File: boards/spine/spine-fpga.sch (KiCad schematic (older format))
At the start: 1 part, among them U2 iCE40-HX1K-TQ144

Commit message: Get the BOM started
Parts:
- U2: MfgId (none) -> ICE40HX1K-TQ144; MfrId (none) -> Lattice; RefPrice1k (none) -> 4.5703; Vend1 (none) -> Digikey; Vend1Id (none) -> 220-1565-ND
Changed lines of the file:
@@
 F 1 "iCE40-HX1K-TQ144" H 1800 1800 60  0000 L CNN
 F 2 "" H 1600 1650 60  0000 C CNN
-F 3 "" H 1600 1650 60  0000 C CNN
+F 3 "http://www.latticesemi.com/~/media/LatticeSemi/Documents/DataSheets/iCE/iCE40LPHXFamilyDataSheet.pdf" H 1600 1650 60  0001 C CNN
+F 4 "4.5703" H 1600 1650 60  0001 C CNN "RefPrice1k"
+F 5 "Lattice" H 1600 1650 60  0001 C CNN "MfrId"
+F 6 "ICE40HX1K-TQ144" H 1600 1650 60  0001 C CNN "MfgId"
+F 7 "220-1565-ND" H 1600 1650 60  0001 C CNN "Vend1Id"
+F 8 "Digikey" H 1600 1650 60  0001 C CNN "Vend1"
 	1    1600 1650
 	1    0    0    -1

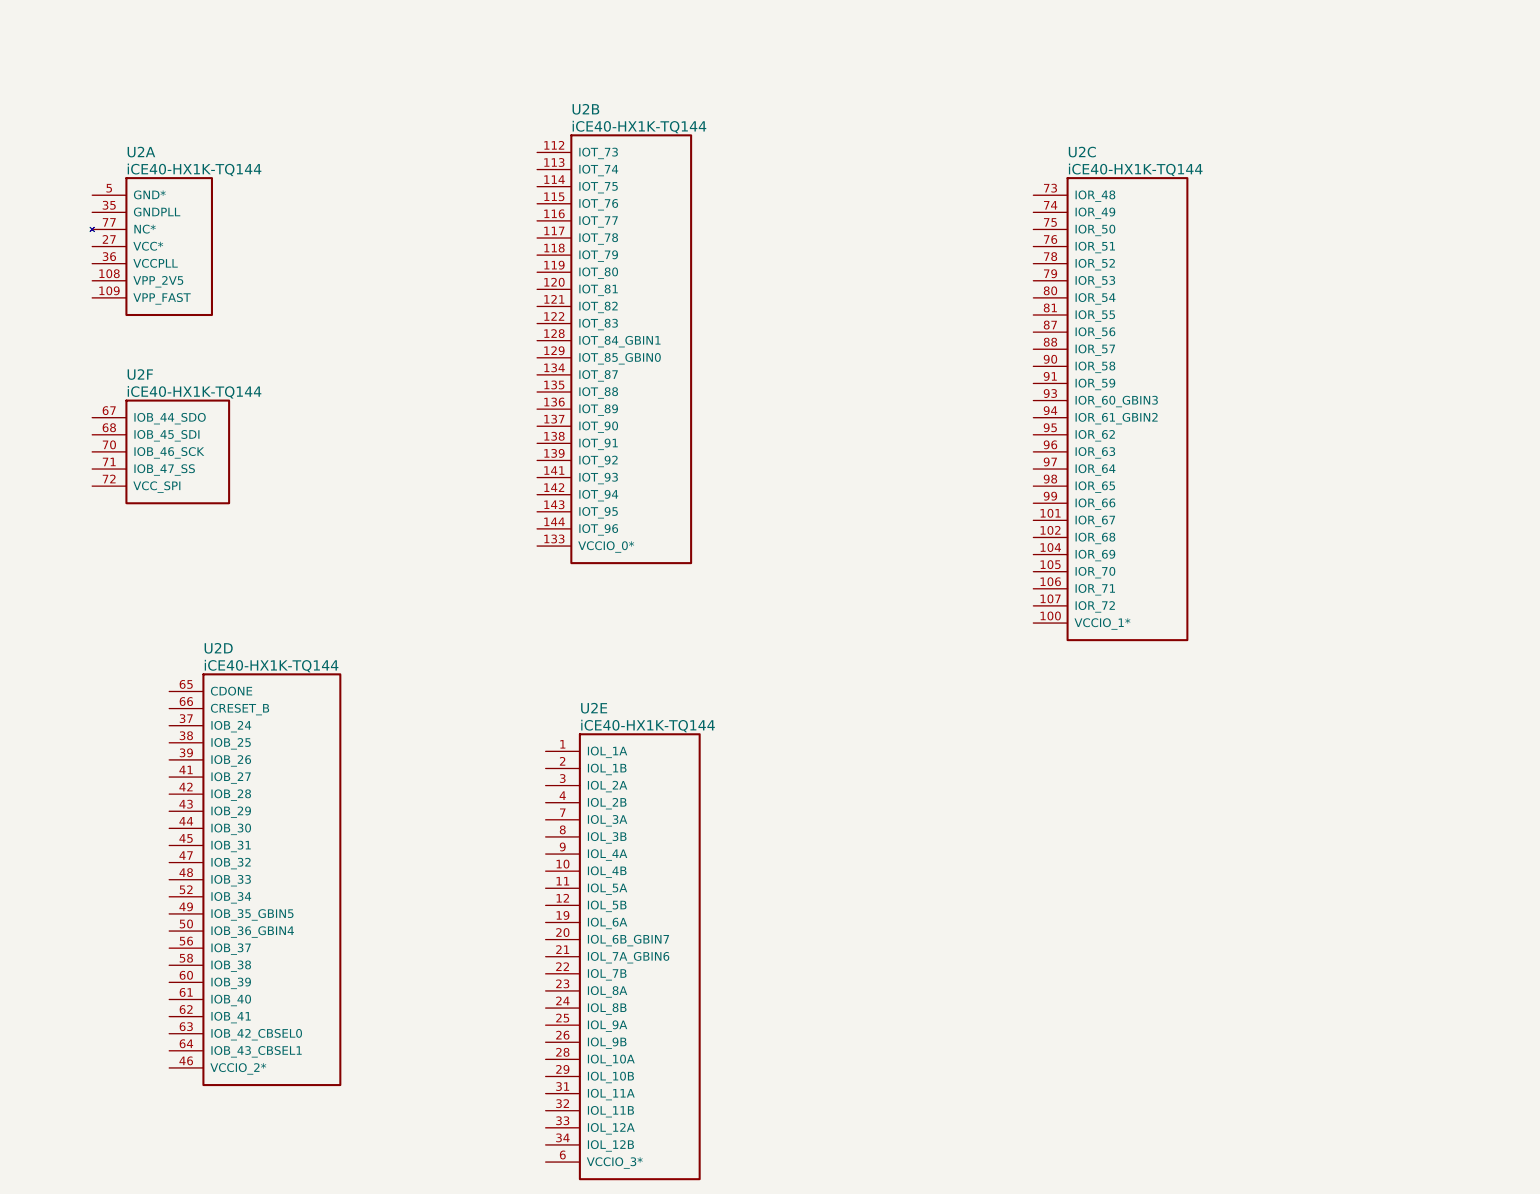
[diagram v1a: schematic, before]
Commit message: USB port: ESD, crystal, eeprom
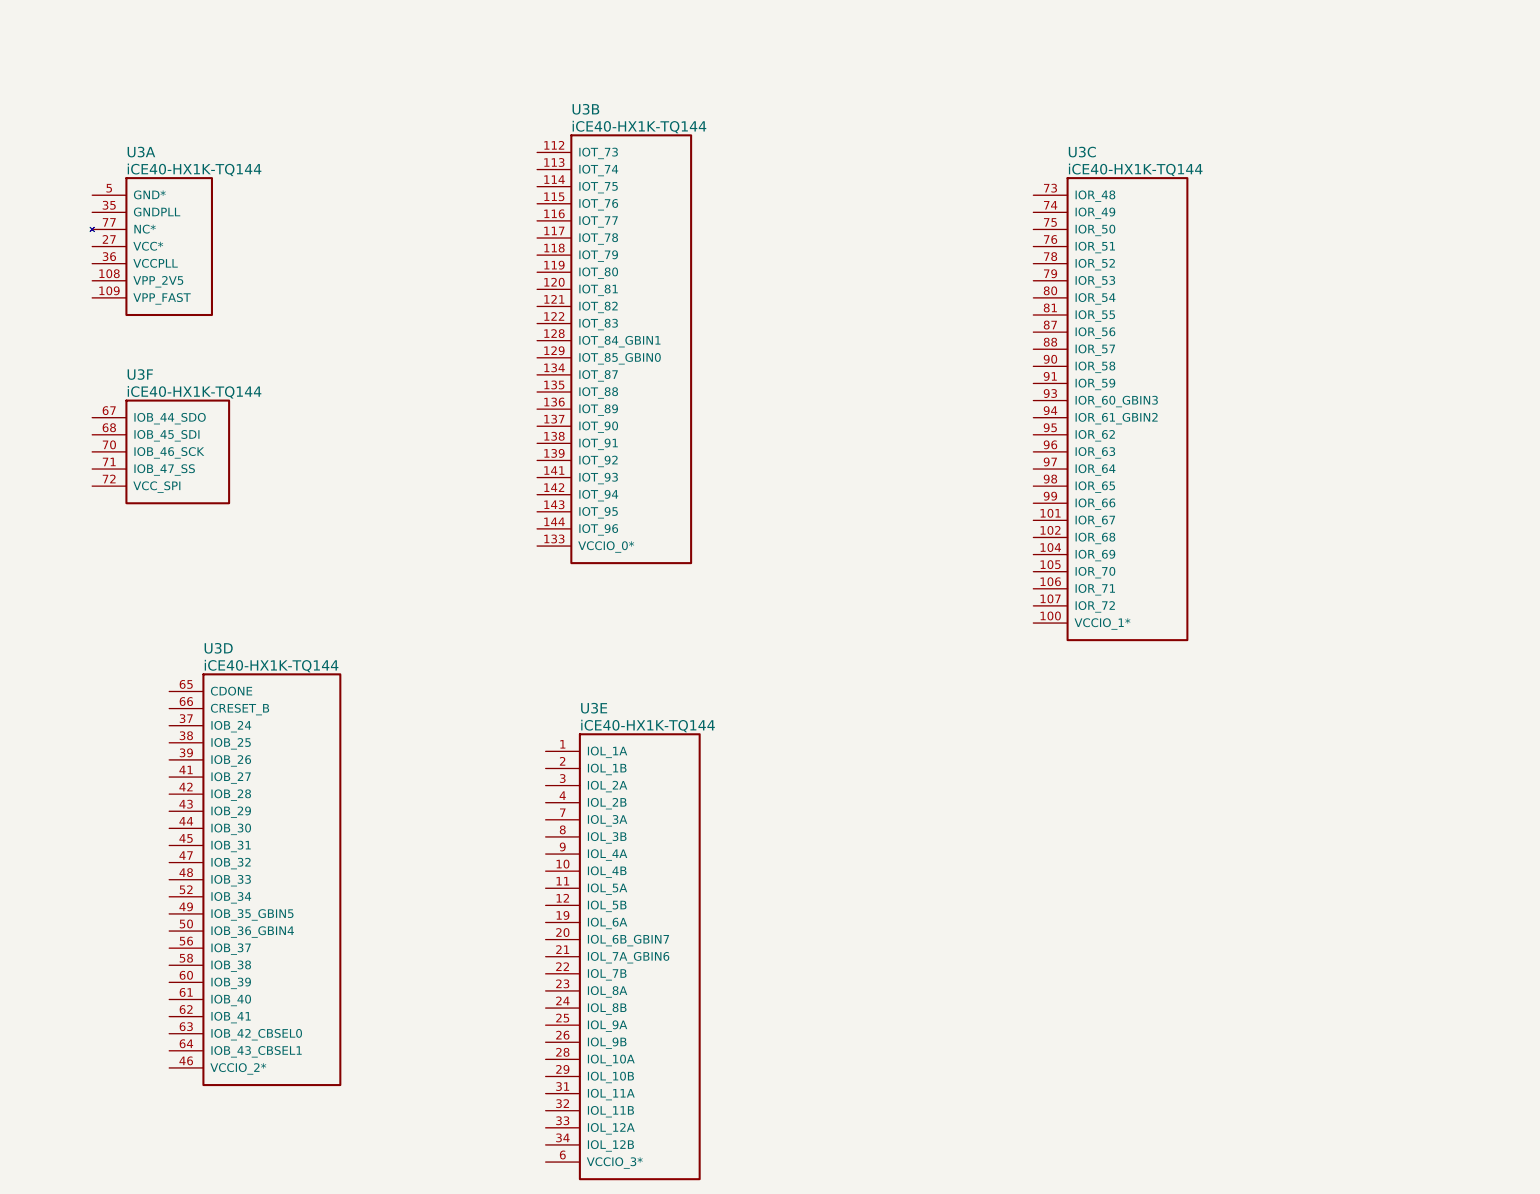
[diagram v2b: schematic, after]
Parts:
- renumbered U2 to U3
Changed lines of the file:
@@
 $EndDescr
 $Comp
-L iCE40-HX1K-TQ144 U2
+L iCE40-HX1K-TQ144 U3
 U 1 1 5637E334
 P 1600 1650
-F 0 "U2" H 1800 1900 60  0000 L CNN
+F 0 "U3" H 1800 1900 60  0000 L CNN
 F 1 "iCE40-HX1K-TQ144" H 1800 1800 60  0000 L CNN
 F 2 "" H 1600 1650 60  0000 C CNN
@@
 $EndComp
 $Comp
-L iCE40-HX1K-TQ144 U2
+L iCE40-HX1K-TQ144 U3
 U 2 1 5637E355
 P 4200 1400
-F 0 "U2" H 4400 1650 60  0000 L CNN
+F 0 "U3" H 4400 1650 60  0000 L CNN
 F 1 "iCE40-HX1K-TQ144" H 4400 1550 60  0000 L CNN
 F 2 "" H 4200 1400 60  0000 C CNN
@@
 $EndComp
 $Comp
-L iCE40-HX1K-TQ144 U2
+L iCE40-HX1K-TQ144 U3
 U 3 1 5637E37F
 P 7100 1650
-F 0 "U2" H 7300 1900 60  0000 L CNN
+F 0 "U3" H 7300 1900 60  0000 L CNN
 F 1 "iCE40-HX1K-TQ144" H 7300 1800 60  0000 L CNN
 F 2 "" H 7100 1650 60  0000 C CNN
@@
 $EndComp
 $Comp
-L iCE40-HX1K-TQ144 U2
+L iCE40-HX1K-TQ144 U3
 U 4 1 5637E3AD
 P 2050 4550
-F 0 "U2" H 2250 4800 60  0000 L CNN
+F 0 "U3" H 2250 4800 60  0000 L CNN
 F 1 "iCE40-HX1K-TQ144" H 2250 4700 60  0000 L CNN
 F 2 "" H 2050 4550 60  0000 C CNN
@@
 $EndComp
 $Comp
-L iCE40-HX1K-TQ144 U2
+L iCE40-HX1K-TQ144 U3
 U 5 1 5637E3E2
 P 4250 4900
-F 0 "U2" H 4450 5150 60  0000 L CNN
+F 0 "U3" H 4450 5150 60  0000 L CNN
 F 1 "iCE40-HX1K-TQ144" H 4450 5050 60  0000 L CNN
 F 2 "" H 4250 4900 60  0000 C CNN
@@
 $EndComp
 $Comp
-L iCE40-HX1K-TQ144 U2
+L iCE40-HX1K-TQ144 U3
 U 6 1 5637E41B
 P 1600 2950
-F 0 "U2" H 1800 3200 60  0000 L CNN
+F 0 "U3" H 1800 3200 60  0000 L CNN
 F 1 "iCE40-HX1K-TQ144" H 1800 3100 60  0000 L CNN
 F 2 "" H 1600 2950 60  0000 C CNN

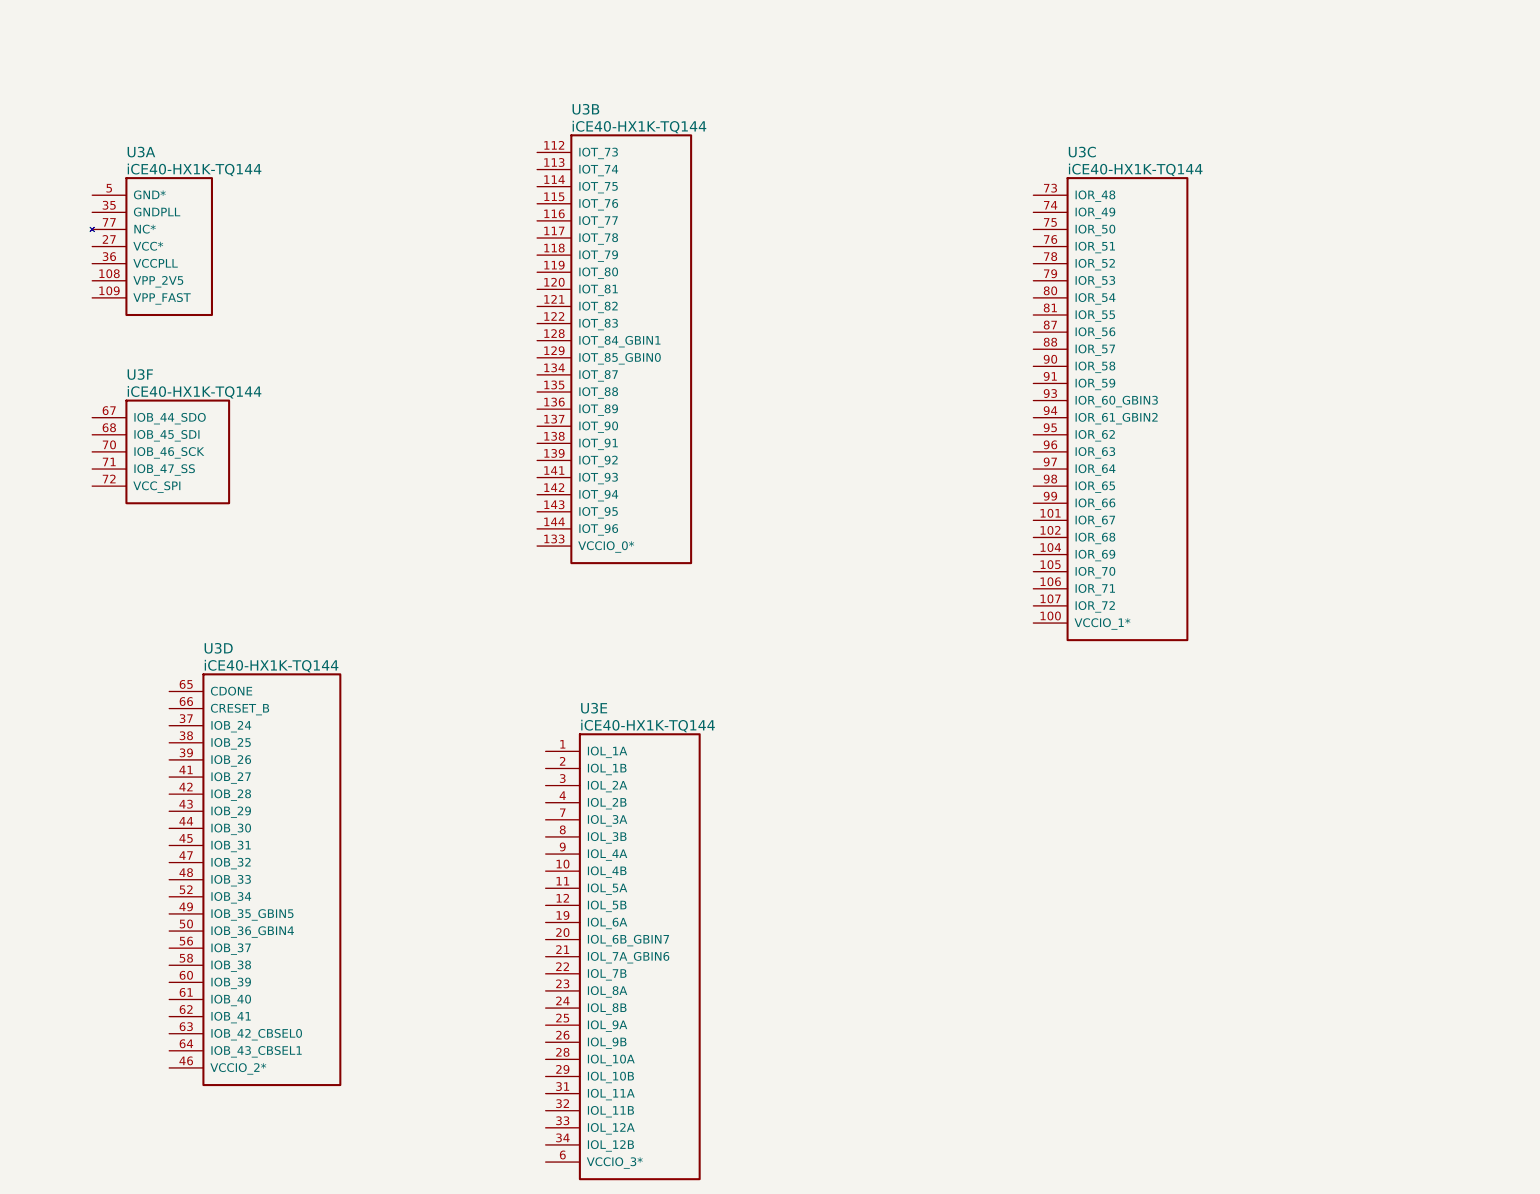
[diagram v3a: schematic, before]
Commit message: Getting the FPGA set up
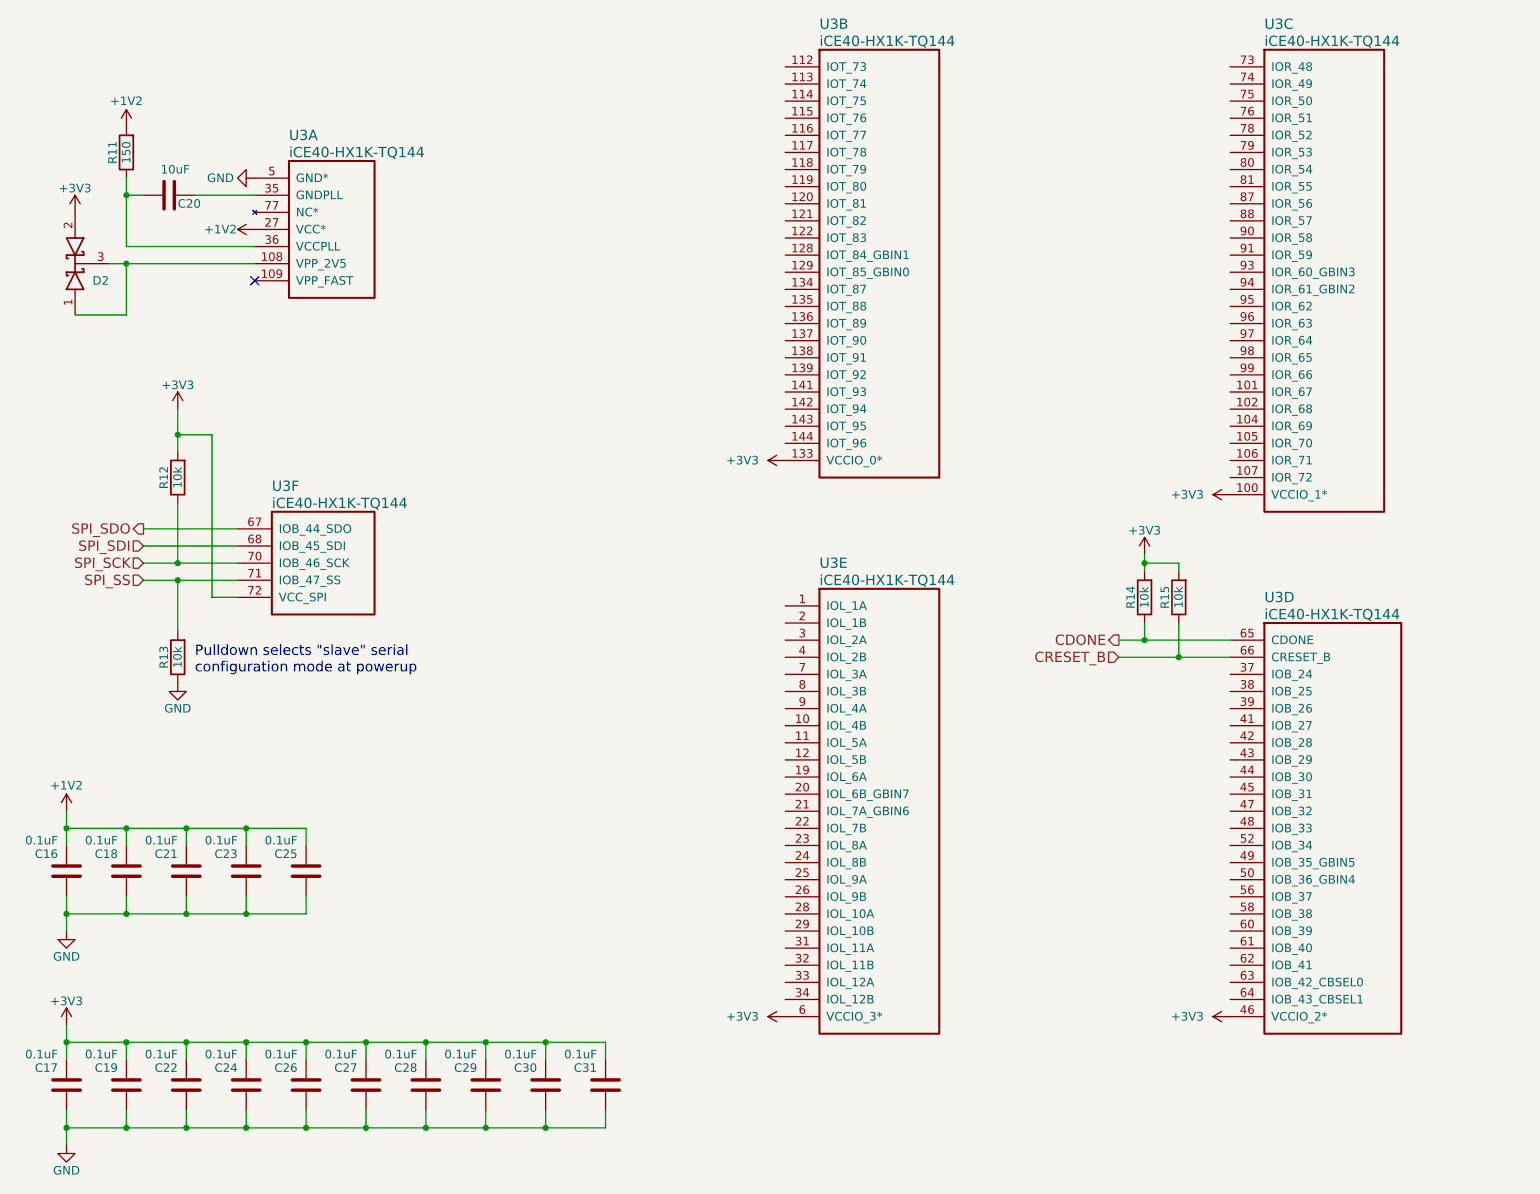
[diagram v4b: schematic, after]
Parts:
- added C16, C17, C18, C19, C21, C22, C23, C24, C25, C26, C27, C28, C29, C30, C31: 0.1uF, symbol C
- added C20: 10uF, symbol C
- added D2: BAT54 2x common cathode, symbol D_Schottky_x2_KCom_AAK
- added R11: 150, symbol R
- added R12, R13, R14, R15: 10k, symbol R
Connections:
- net GND: now reaches U3.103 (GND*), U3.13 (GND*), U3.132 (GND*), U3.14 (GND*), U3.140 (GND*), U3.5 (GND*), U3.59 (GND*), U3.69 (GND*), U3.86 (GND*)
- net GND: now also C16.1, C17.1, C18.1, C19.1, C21.1, C22.1, C23.1, C24.1, C25.1, C26.1, C27.1, C28.1, C29.1, C30.1, C31.1, R13.1
- net at U3.108 (VPP_2V5): now also D2.1 (A), D2.3 (K)
- net +1V2: now reaches U3.111 (VCC*), U3.27 (VCC*), U3.51 (VCC*), U3.92 (VCC*)
- net +1V2: now also C16.2, C18.2, C21.2, C23.2, C25.2, R11.2
- net at U3.35 (GNDPLL): now also C20.1
- net at U3.36 (VCCPLL): now also C20.2, R11.1
- net +3V3: now reaches U3.123 (VCCIO_0*), U3.133 (VCCIO_0*)
- net +3V3: now also U3.100 (VCCIO_1*), U3.30 (VCCIO_3*), U3.46 (VCCIO_2*), U3.57 (VCCIO_2*), U3.6 (VCCIO_3*), U3.72 (VCC_SPI), U3.89 (VCCIO_1*), C17.2, C19.2, C22.2, C24.2, C26.2, C27.2, C28.2, C29.2, C30.2, C31.2, D2.2 (A), R12.2, R14.2, R15.2
- net CDONE: now reaches U3.65 (CDONE)
- net CDONE: now also R14.1
- net CRESET_B: now reaches U3.66 (CRESET_B)
- net CRESET_B: now also R15.1
- net SPI_SDO: now reaches U3.67 (IOB_44_SDO)
- net SPI_SDI: now reaches U3.68 (IOB_45_SDI)
- net SPI_SCK: now reaches U3.70 (IOB_46_SCK)
- net SPI_SCK: now also R12.1
- net SPI_SS: now reaches U3.71 (IOB_47_SS)
- net SPI_SS: now also R13.2
- no-connect marks 0 -> 1
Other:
- note added: "Pulldown selects "slave" serial\nconfiguration mode at powerup"
- moved on the sheet: U3A, U3B, U3C, U3D, U3E, U3F

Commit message: Pick better capacitors :)
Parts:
- removed C16, C17, C18, C19, C21, C22, C23, C24, C25, C26, C27, C28: 0.1uF, symbol C
- removed C20: 10uF, symbol C
- added C32, C33, C35, C36, C37, C38, C39, C40, C41, C42, C43, C44, C45: 0.1uF, 0805, symbol C
- added C34: 10uF, 1206, symbol C
- C29, C30, C31: footprint (none) -> 0805; MfgId CC0805ZRY5V9BB104 -> GRM21BR71H104MA01L; MfrId Yageo -> Murata; RefPrice1k 0.00783 -> 0.01880; Vend1Id 311-1361-1-ND -> 490-9672-2-ND
- renumbered D2 to D5, R11 to R15, R12 to R16, R13 to R17, R14 to R18, R15 to R19, U3 to U7
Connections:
- net +1V2: now also C29.2, C31.2, C35.2, C37.2, C39.2
- net +3V3: now also C32.2, C36.2, C38.2, C40.2, C41.2, C42.2, C43.2, C44.2, C45.2; no longer C29.2, C31.2
- net GND: now also C32.1, C35.1, C36.1, C37.1, C38.1, C39.1, C40.1, C41.1, C42.1, C43.1, C44.1, C45.1
- net at D5.3 (K), U7.108 (VPP_2V5): no longer D5.1 (A)
- net at U7.35 (GNDPLL): now also C33.1, C34.2
- net at R15.1, U7.36 (VCCPLL): now also C33.2, C34.1
- no-connect marks 1 -> 2
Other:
- moved on the sheet: D5, R15, R16, R17, R18, R19, U7A, U7B, U7C, U7D, U7E, U7F
